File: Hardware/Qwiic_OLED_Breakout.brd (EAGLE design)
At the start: 27.3 x 34.3 mm, 29 parts

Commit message: fixed vscore
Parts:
- moved H1 4.57 mm to (21.0, 27.2)
- moved H2 4.57 mm to (-0.64, 27.2)
- moved LOGO4 4.57 mm to (4.57, 21.1)
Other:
- board size 27.3 x 34.3 mm -> 27.3 x 29.7 mm
- board text removed: "Vcut"
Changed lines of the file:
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@@
 <setting verticaltext="up"/>
 </settings>
-<grid distance="0.05" unitdist="inch" unit="inch" style="lines" multiple="1" display="yes" altdistance="0.005" altunitdist="inch" altunit="inch"/>
+<grid distance="0.01" unitdist="inch" unit="inch" style="lines" multiple="1" display="yes" altdistance="0.005" altunitdist="inch" altunit="inch"/>
 <layers>
 <layer number="1" name="Top" color="4" fill="1" visible="yes" active="yes"/>
@@
 <wire x1="0" y1="20.32" x2="0" y2="0" width="0.2032" layer="20"/>
 <wire x1="0" y1="0" x2="20.32" y2="0" width="0.2032" layer="20"/>
-<wire x1="-3.556" y1="34.29" x2="-3.556" y2="29.21" width="0.2032" layer="20"/>
-<wire x1="-3.556" y1="29.21" x2="1.905" y2="29.21" width="0.2032" layer="20"/>
-<wire x1="18.415" y1="29.21" x2="23.749" y2="29.21" width="0.2032" layer="20"/>
-<wire x1="23.749" y1="29.21" x2="23.749" y2="34.29" width="0.2032" layer="20"/>
-<rectangle x1="6.16" y1="30.13" x2="14.16" y2="32.13" layer="46" rot="R180"/>
-<rectangle x1="12.16" y1="32.13" x2="14.16" y2="34.13" layer="46" rot="R180"/>
-<wire x1="12.16" y1="34.29" x2="12.16" y2="32.13" width="0.2032" layer="20"/>
-<wire x1="12.16" y1="32.13" x2="6.16" y2="32.13" width="0.2032" layer="20"/>
-<wire x1="6.16" y1="32.13" x2="6.16" y2="30.13" width="0.2032" layer="20"/>
-<wire x1="6.16" y1="30.13" x2="14.16" y2="30.13" width="0.2032" layer="20"/>
-<wire x1="12.16" y1="34.29" x2="-3.556" y2="34.29" width="0.2032" layer="20"/>
-<wire x1="14.163040625" y1="30.134559375" x2="14.163040625" y2="34.29" width="0.2032" layer="20"/>
-<wire x1="14.163040625" y1="34.29" x2="23.749" y2="34.29" width="0.2032" layer="20"/>
+<wire x1="-3.556" y1="29.718" x2="-3.556" y2="24.638" width="0.2032" layer="20"/>
+<wire x1="-3.556" y1="24.638" x2="1.905" y2="24.638" width="0.2032" layer="20"/>
+<wire x1="18.415" y1="24.638" x2="23.749" y2="24.638" width="0.2032" layer="20"/>
+<wire x1="23.749" y1="24.638" x2="23.749" y2="29.718" width="0.2032" layer="20"/>
+<rectangle x1="6.16" y1="25.558" x2="14.16" y2="27.558" layer="46" rot="R180"/>
+<rectangle x1="12.16" y1="27.558" x2="14.16" y2="29.558" layer="46" rot="R180"/>
+<wire x1="12.16" y1="29.718" x2="12.16" y2="27.558" width="0.2032" layer="20"/>
+<wire x1="12.16" y1="27.558" x2="6.16" y2="27.558" width="0.2032" layer="20"/>
+<wire x1="6.16" y1="27.558" x2="6.16" y2="25.558" width="0.2032" layer="20"/>
+<wire x1="6.16" y1="25.558" x2="14.16" y2="25.558" width="0.2032" layer="20"/>
+<wire x1="12.16" y1="29.718" x2="-3.556" y2="29.718" width="0.2032" layer="20"/>
+<wire x1="14.163040625" y1="25.562559375" x2="14.163040625" y2="29.718" width="0.2032" layer="20"/>
+<wire x1="14.163040625" y1="29.718" x2="23.749" y2="29.718" width="0.2032" layer="20"/>
 <text x="8.89" y="-27.94" size="1.778" layer="51" font="vector">Joel Bartlett</text>
-<dimension x1="-3.81" y1="34.29" x2="-3.81" y2="0" x3="-15.24" y3="17.145" textsize="1.778" layer="47" unit="inch"/>
-<dimension x1="-3.556" y1="34.29" x2="23.749" y2="34.29" x3="10.0965" y3="40.64" textsize="1.778" layer="47" unit="inch"/>
-<dimension x1="-0.635" y1="31.75" x2="20.955" y2="31.75" x3="10.16" y3="36.83" textsize="1.778" layer="47" unit="inch"/>
-<dimension x1="0" y1="0" x2="0" y2="31.75" x3="-11.43" y3="15.875" textsize="1.778" layer="47" unit="inch"/>
+<dimension x1="-3.81" y1="29.718" x2="-3.81" y2="0" x3="-15.24" y3="14.859" textsize="1.778" layer="47" unit="inch"/>
+<dimension x1="-3.556" y1="29.718" x2="23.749" y2="29.718" x3="10.0965" y3="36.068" textsize="1.778" layer="47" unit="inch"/>
+<dimension x1="-0.635" y1="27.178" x2="20.955" y2="27.178" x3="10.16" y3="32.258" textsize="1.778" layer="47" unit="inch"/>
+<dimension x1="0" y1="0" x2="0" y2="27.178" x3="-11.43" y3="13.589" textsize="1.778" layer="47" unit="inch"/>
 <text x="12.7" y="-30.48" size="1.778" layer="51" font="vector">Andy England</text>
-<wire x1="-1.27" y1="22.86" x2="21.59" y2="22.86" width="0.2032" layer="20"/>
-<wire x1="1.905" y1="29.21" x2="1.905" y2="25.4" width="0.2032" layer="20"/>
-<wire x1="1.905" y1="25.4" x2="18.415" y2="25.4" width="0.2032" layer="20"/>
-<wire x1="18.415" y1="25.4" x2="18.415" y2="29.21" width="0.2032" layer="20"/>
+<wire x1="1.905" y1="24.638" x2="1.905" y2="20.828" width="0.2032" layer="20"/>
+<wire x1="1.905" y1="20.828" x2="18.415" y2="20.828" width="0.2032" layer="20"/>
+<wire x1="18.415" y1="20.828" x2="18.415" y2="24.638" width="0.2032" layer="20"/>
 <wire x1="0" y1="20.32" x2="20.32" y2="20.32" width="0.2032" layer="20"/>
-<text x="-3.81" y="22.86" size="1.778" layer="20" align="center">Vcut</text>
-<dimension x1="-6.35" y1="22.86" x2="-6.35" y2="0" x3="-7.62" y3="11.43" textsize="1.778" layer="20" unit="inch"/>
 </plain>
 <attributes>
@@
 </element>
 <element name="JP2" library="SparkFun-Jumpers" package="SMT-JUMPER_3_2-NC_PASTE_SILK" value="" x="6.985" y="12.7" rot="R180"/>
-<element name="H1" library="SparkFun-Hardware" package="STAND-OFF" value="STAND-OFF" x="20.955" y="31.75"/>
-<element name="H2" library="SparkFun-Hardware" package="STAND-OFF" value="STAND-OFF" x="-0.635" y="31.75"/>
+<element name="H1" library="SparkFun-Hardware" package="STAND-OFF" value="STAND-OFF" x="20.955" y="27.178"/>
+<element name="H2" library="SparkFun-Hardware" package="STAND-OFF" value="STAND-OFF" x="-0.635" y="27.178"/>
 <element name="JP3" library="SparkFun-Jumpers" package="SMT-JUMPER_2_NO_SILK" value="" x="12.7" y="12.7"/>
 <element name="LOGO1" library="SparkFun-Aesthetics" package="REVISION" value="REVISION" x="-6.35" y="-30.48"/>
 <element name="LOGO2" library="SparkFun-Aesthetics" package="SFE_LOGO_FLAME_.1" value="SFE_LOGO_FLAME.1_INCH" x="2.032" y="0.762"/>
-<element name="LOGO4" library="SparkFun-Aesthetics" package="SFE_LOGO_NAME_.1" value="SFE_LOGO_NAME.1_INCH" x="4.572" y="25.654"/>
+<element name="LOGO4" library="SparkFun-Aesthetics" package="SFE_LOGO_NAME_.1" value="SFE_LOGO_NAME.1_INCH" x="4.572" y="21.082"/>
 <element name="FID3" library="SparkFun-Aesthetics" package="FIDUCIAL-1X2" value="FIDUCIAL1X2" x="1.27" y="15.875" rot="MR0"/>
 <element name="FID4" library="SparkFun-Aesthetics" package="FIDUCIAL-1X2" value="FIDUCIAL1X2" x="19.05" y="1.27" rot="MR0"/>

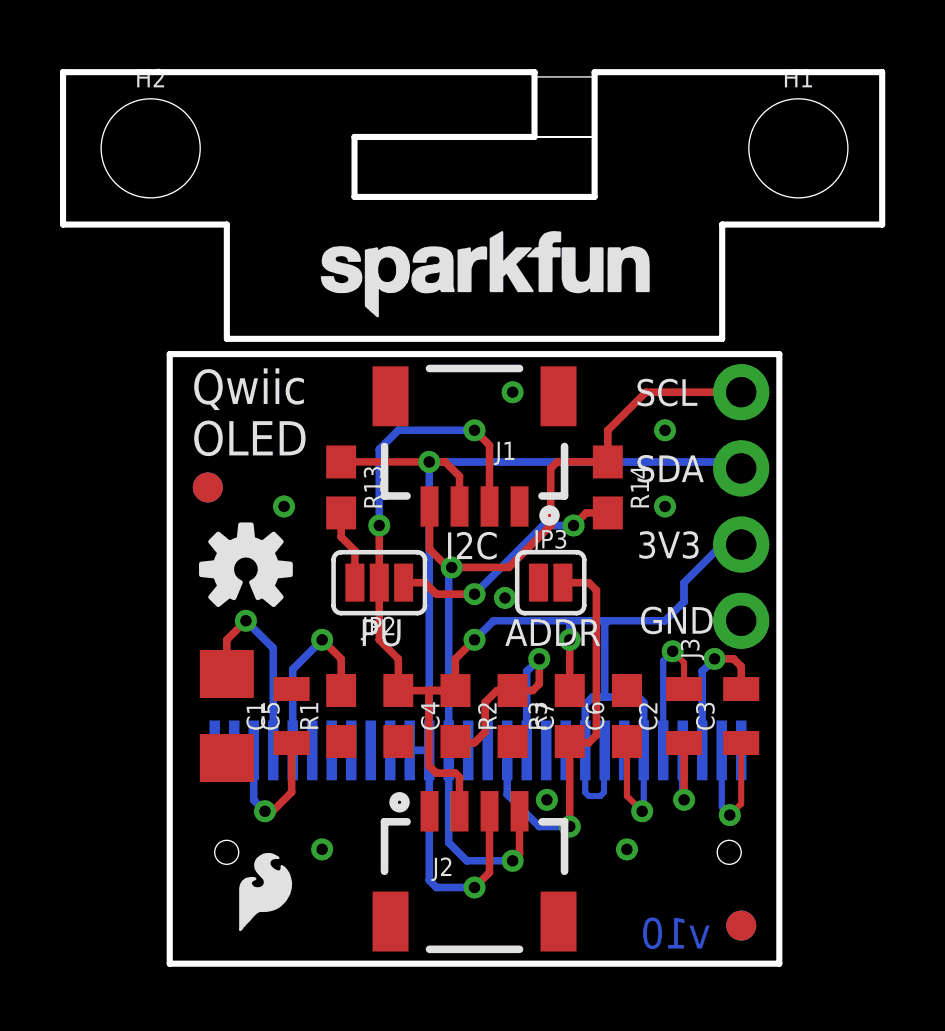
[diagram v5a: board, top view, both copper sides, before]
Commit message: Expands the distance between the standoff 0.5" to adhere to our Qwiic standard
* Updates silk
* Organizes schematic
* Adds ordering instructions
* Adds additional measures and units for the measures
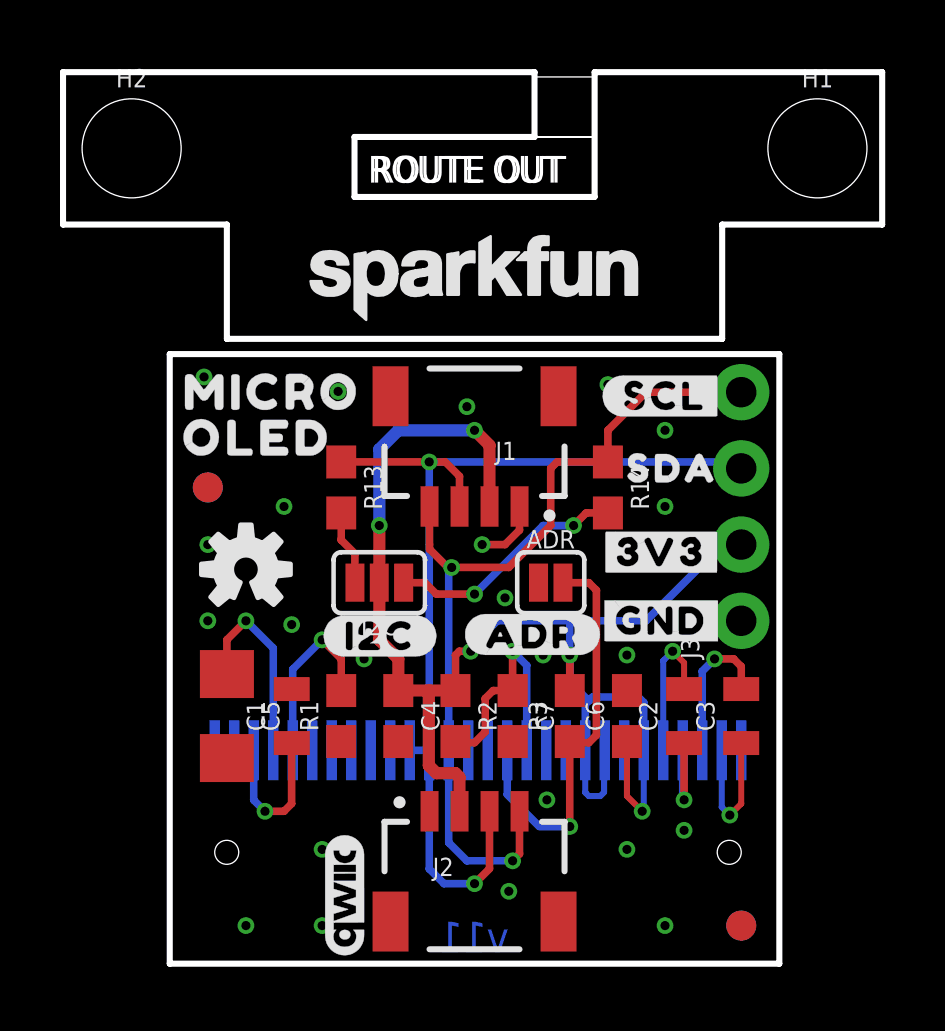
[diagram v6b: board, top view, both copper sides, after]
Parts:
- added LOGO5: QWIIC_LOGO_4MM, SparkFun-Aesthetics:QWIIC_4MM
- added LOGO6: SPECIAL_INSTRUCTIONS-ORDERING, SparkFun-Aesthetics:ORDERING_INSTRUCTIONS
- added U$1, U$13: (no value), pot:MICRO593420
- added U$10: (no value), botmirror:#SDA#10
- added U$11, U$5: (no value), pot:#3V3#1
- added U$12, U$6: (no value), pot:#GND#0
- added U$14, U$2: (no value), pot:OLED593421
- added U$3: (no value), pot:#ADR#5
- added U$4: (no value), bot:#SCL#9
- added U$7: (no value), pot:SDA8
- added U$8: (no value), topmirror:#I2C#1348
- added U$9: (no value), top:#SCL#8
- I2C: value (none) -> JUMPER-SMT_3_2-NC_PASTE_SILK
- J1, J2: value (none) -> QWIIC_RIGHT_ANGLE; device SparkFun-Connectors:1X04_1MM_RA -> SparkFun-Connectors:JST04_1MM_RA
- LOGO2: value SFE_LOGO_FLAME.1_INCH -> SFE_LOGO_NAME.1_INCH; device SparkFun-Aesthetics:SFE_LOGO_FLAME_.1 -> SparkFun-Aesthetics:SFE_LOGO_NAME_.1
- moved LOGO2 23.5 mm to (10.2, 22.9)
- moved LOGO4 3.35 mm to (6.60, 18.4), flipped to the bottom
- moved H1 0.64 mm to (21.6, 27.2)
- moved H2 0.64 mm to (-1.27, 27.2)
- renumbered JP2 to I2C, JP3 to ADR
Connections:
- net D0/SCK renamed D0/SCL/SCK
- net D1/MOSI renamed D1/SDA/PICO
- removed net CS: OLED1.11
- removed net D3: OLED1.19
- removed net D4: OLED1.20
- removed net D5: OLED1.21
- removed net D6: OLED1.22
- removed net D7: OLED1.23
- removed net RD/E: OLED1.15
- removed net WR/RW: OLED1.14
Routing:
- net GND: track 0.00 -> 2.23 mm, vias 8 -> 23
- net VDD: track 52.9 -> 51.9 mm
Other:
- board text added: "1.6mm Thickness"
- board text added: "Andy England, Elias Santistevan"
- board text added: "Lead-Free HASL"
- board text added: "ROUTE OUT"
- board text added: "Red Silk"
- board text added: "Two Layer Board"
- board text added: "Units in Inches"
- board text added: "White Silkscreen"
- board text added: "v11"
- board text removed: "3V3"
- board text removed: "ADDR"
- board text removed: "Andy England"
- board text removed: "GND"
- board text removed: "I2C"
- board text removed: "PU"
- board text removed: "Qwiic OLED"
- board text removed: "Qwiic OLED Breakout"
- board text removed: "SCL"
- board text removed: "SDA"
- board text removed: "v10"

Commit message: Updates jumper library
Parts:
- ADR: value (none) -> JUMPER-SMT_2_NO_SILK
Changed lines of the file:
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@@
 <setting verticaltext="up"/>
 </settings>
-<grid distance="0.05" unitdist="inch" unit="inch" style="dots" multiple="1" display="yes" altdistance="0.001" altunitdist="inch" altunit="inch"/>
+<grid distance="0.05" unitdist="inch" unit="inch" style="dots" multiple="1" display="yes" altdistance="0.005" altunitdist="inch" altunit="inch"/>
 <layers>
 <layer number="1" name="Top" color="4" fill="1" visible="yes" active="yes"/>
@@
 <attribute name="VALUE" x="-1.27" y="25.146" size="0.6096" layer="27" font="vector" ratio="20" align="top-center"/>
 </element>
-<element name="ADR" library="SparkFun-Jumpers" package="SMT-JUMPER_2_NO_SILK" value="" x="12.7" y="12.7" smashed="yes">
+<element name="ADR" library="SparkFun-Jumpers" package="SMT-JUMPER_2_NO_SILK" package3d_urn="urn:adsk.eagle:package:39279/1" value="JUMPER-SMT_2_NO_SILK" x="12.7" y="12.7" smashed="yes">
 <attribute name="NAME" x="12.7" y="13.843" size="0.6096" layer="25" font="vector" ratio="20" align="bottom-center"/>
 <attribute name="VALUE" x="12.7" y="11.557" size="0.6096" layer="27" font="vector" ratio="20" align="top-center"/>

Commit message: Updates D/C net
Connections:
- net D/C renamed D/!C!
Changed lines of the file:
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@@
 <wire x1="3.81" y1="5.08" x2="3.175" y2="5.08" width="0.254" layer="1"/>
 </signal>
-<signal name="D/C">
+<signal name="D/!C!">
 <contactref element="OLED1" pad="13"/>
 <contactref element="ADR" pad="2"/>
